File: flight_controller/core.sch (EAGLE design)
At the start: 119 parts, among them J1 M02, J10 M02, J11 M03, J12 M02, J13 M02, J14 M02, J15 M03, J16 M03, J17 M03, J18 M04, J19 M04, J2 M02, J20 M03, J21 M04, J3 M02, J4 M03, J5 M02, J6 M02, J7 M02, J8 M02, J9 M03, Q1 EM6K1, Q2 EM6K1, Q3 EM6K1, Q4 EM6K1, Q5 EM6K1, Q6 EM6K1, Q7 MOSFET-PCHANNEL-AON6407, U1 STM32F405, U2 MEAS-MS5611, U3 MPU-9250-QFN-24-NP, U4 MIC5219 3.3V, U5 USD-SOCKETNEW, Y1 16MHz

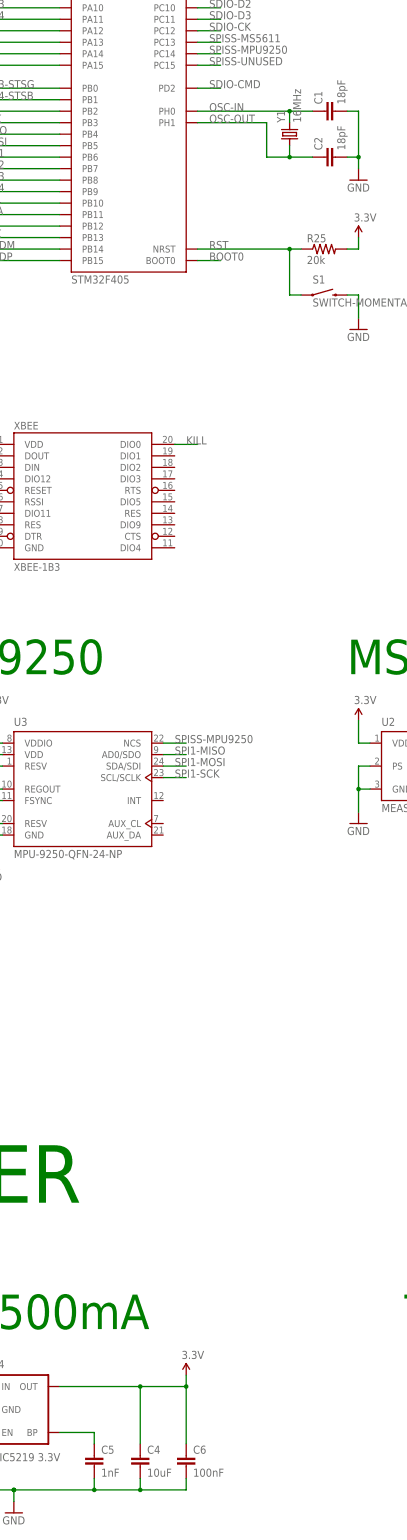
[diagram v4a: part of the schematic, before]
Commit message: Layout 70% done with new 8MHz crystal.
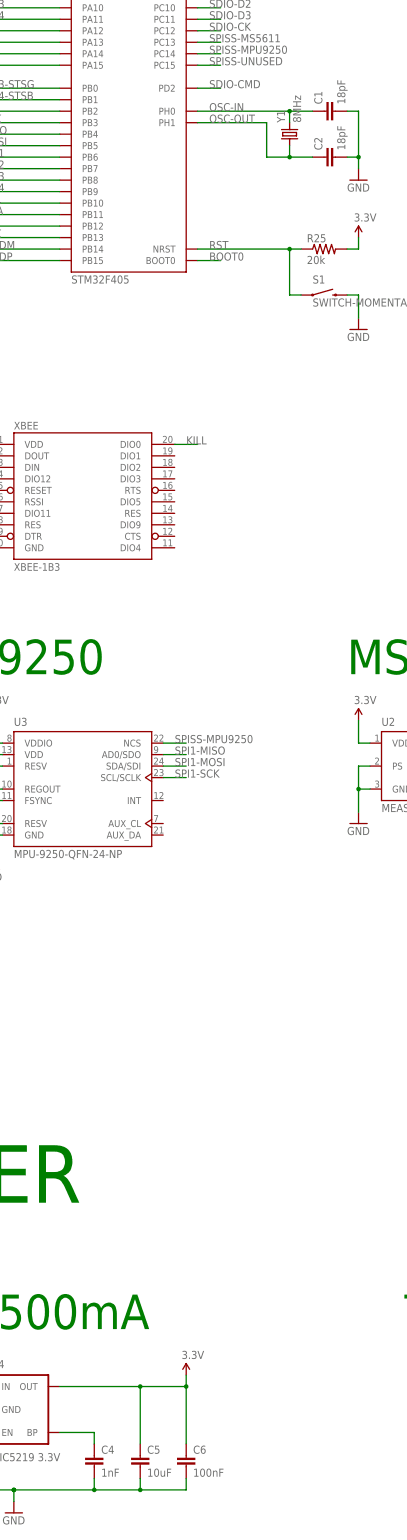
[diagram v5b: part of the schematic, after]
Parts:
- C4: value 10uF -> 1nF; device OSURC_Passives:CAP-10UF-10V-10%(0805) -> OSURC_Passives:CAP-1NF-50V-10%(0603)
- C5: value 1nF -> 10uF; device OSURC_Passives:CAP-1NF-50V-10%(0603) -> OSURC_Passives:CAP-10UF-10V-10%(0805)
- Y1: value 16MHz -> 8MHz; device SparkFun-FreqCtrl:CRYSTAL5X3 -> OSURC_FreqCtrl:CRYSTAL-8MHZ-CX532
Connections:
- net 3.3V: now also C5.2; no longer C4.2
- net MIC-BP: now also C4.2; no longer C5.2
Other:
- moved on the sheet: C4, C5
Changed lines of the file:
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@@
 <part name="C6" library="OSURC_Passives" deviceset="CAP" device="-100NF-16V-10%(0603)" value="100nF"/>
 <part name="U4" library="SparkFun-PowerIC" deviceset="V_REG_MIC5219" device="3.3V" value="MIC5219 3.3V"/>
-<part name="C5" library="OSURC_Passives" deviceset="CAP" device="-1NF-50V-10%(0603)" value="1nF"/>
+<part name="C4" library="OSURC_Passives" deviceset="CAP" device="-1NF-50V-10%(0603)" value="1nF"/>
 <part name="SUPPLY2" library="SparkFun-Aesthetics" deviceset="5V" device=""/>
 <part name="SUPPLY6" library="SparkFun-Aesthetics" deviceset="3.3V" device=""/>
@@
 <part name="R32" library="OSURC_Passives" deviceset="RES" device="-20KOHM-0.1W-1%(0603)" value="20k"/>
 <part name="GND25" library="SparkFun-Aesthetics" deviceset="GND" device=""/>
-<part name="Y1" library="SparkFun-FreqCtrl" deviceset="CRYSTAL" device="5X3" value="16MHz"/>
+<part name="Y1" library="OSURC_FreqCtrl" deviceset="CRYSTAL" device="-8MHZ-CX532" value="8MHz"/>
 <part name="C1" library="OSURC_Passives" deviceset="CAP" device="-18PF-50V-5%(0603)" value="18pF"/>
 <part name="C2" library="OSURC_Passives" deviceset="CAP" device="-18PF-50V-5%(0603)" value="18pF"/>
@@
 <part name="GND6" library="SparkFun-Aesthetics" deviceset="GND" device=""/>
 <part name="C3" library="OSURC_Passives" deviceset="CAP" device="-10UF-10V-10%(0805)" value="10uF"/>
-<part name="C4" library="OSURC_Passives" deviceset="CAP" device="-10UF-10V-10%(0805)" value="10uF"/>
+<part name="C5" library="OSURC_Passives" deviceset="CAP" device="-10UF-10V-10%(0805)" value="10uF"/>
 </parts>
 <sheets>
@@
 <instance part="C6" gate="G$1" x="81.28" y="-104.14"/>
 <instance part="U4" gate="G$1" x="45.72" y="-91.44"/>
-<instance part="C5" gate="G$1" x="60.96" y="-104.14"/>
+<instance part="C4" gate="G$1" x="60.96" y="-104.14"/>
 <instance part="SUPPLY2" gate="G$1" x="17.78" y="-83.82"/>
 <instance part="SUPPLY6" gate="G$1" x="81.28" y="-83.82"/>
@@
 <instance part="GND6" gate="1" x="363.22" y="-629.92"/>
 <instance part="C3" gate="G$1" x="17.78" y="-104.14"/>
-<instance part="C4" gate="G$1" x="71.12" y="-104.14"/>
+<instance part="C5" gate="G$1" x="71.12" y="-104.14"/>
 </instances>
 <busses>
@@
 <wire x1="17.78" y1="-109.22" x2="30.48" y2="-109.22" width="0.1524" layer="91"/>
 <junction x="30.48" y="-109.22"/>
-<pinref part="C5" gate="G$1" pin="1"/>
+<pinref part="C4" gate="G$1" pin="1"/>
 <wire x1="60.96" y1="-106.68" x2="60.96" y2="-109.22" width="0.1524" layer="91"/>
 <junction x="60.96" y="-109.22"/>
 <pinref part="GND8" gate="1" pin="GND"/>
 <pinref part="C3" gate="G$1" pin="1"/>
-<pinref part="C4" gate="G$1" pin="1"/>
+<pinref part="C5" gate="G$1" pin="1"/>
 </segment>
 <segment>
@@
 <pinref part="SUPPLY6" gate="G$1" pin="3.3V"/>
 <junction x="81.28" y="-86.36"/>
-<pinref part="C4" gate="G$1" pin="2"/>
+<pinref part="C5" gate="G$1" pin="2"/>
 </segment>
 <segment>
@@
 <segment>
 <pinref part="U4" gate="G$1" pin="BP"/>
-<pinref part="C5" gate="G$1" pin="2"/>
+<pinref part="C4" gate="G$1" pin="2"/>
 <wire x1="53.34" y1="-96.52" x2="60.96" y2="-96.52" width="0.1524" layer="91"/>
 <wire x1="60.96" y1="-96.52" x2="60.96" y2="-99.06" width="0.1524" layer="91"/>

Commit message: FC layout 90% done.
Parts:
- removed TP15: TEST-POINT-KEYSTONE-5019, OSURC_Passives:TEST-POINT-KEYSTONE-5019
- TP1, TP7, TP8: value TEST-POINT-KEYSTONE-5019 -> TEST-POINT-PAD.03C; device OSURC_Passives:TEST-POINT-KEYSTONE-5019 -> OSURC_Passives:TEST-POINT-PAD.03C
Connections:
- net OSC-IN: no longer TP15.1
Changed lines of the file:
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@@
 <part name="SUPPLY9" library="SparkFun-Aesthetics" deviceset="3.3V" device=""/>
 <part name="SUPPLY23" library="SparkFun-Aesthetics" deviceset="3.3V" device=""/>
-<part name="TP1" library="OSURC_Passives" deviceset="TEST-POINT" device="-KEYSTONE-5019"/>
+<part name="TP1" library="OSURC_Passives" deviceset="TEST-POINT" device="-PAD.03C" value="TEST-POINT-PAD.03C"/>
 <part name="TP2" library="OSURC_Passives" deviceset="TEST-POINT" device="-KEYSTONE-5019"/>
 <part name="TP3" library="OSURC_Passives" deviceset="TEST-POINT" device="-KEYSTONE-5019"/>
-<part name="TP7" library="OSURC_Passives" deviceset="TEST-POINT" device="-KEYSTONE-5019"/>
-<part name="TP8" library="OSURC_Passives" deviceset="TEST-POINT" device="-KEYSTONE-5019"/>
+<part name="TP7" library="OSURC_Passives" deviceset="TEST-POINT" device="-PAD.03C" value="TEST-POINT-PAD.03C"/>
+<part name="TP8" library="OSURC_Passives" deviceset="TEST-POINT" device="-PAD.03C" value="TEST-POINT-PAD.03C"/>
 <part name="TP9" library="OSURC_Passives" deviceset="TEST-POINT" device="-KEYSTONE-5019"/>
 <part name="TP10" library="OSURC_Passives" deviceset="TEST-POINT" device="-KEYSTONE-5019"/>
@@
 <part name="TP5" library="OSURC_Passives" deviceset="TEST-POINT" device="-PAD.03C"/>
 <part name="TP6" library="OSURC_Passives" deviceset="TEST-POINT" device="-PAD.03C"/>
-<part name="TP15" library="OSURC_Passives" deviceset="TEST-POINT" device="-KEYSTONE-5019"/>
 <part name="J6" library="OSURC_Connectors" deviceset="M02" device=""/>
 <part name="J10" library="OSURC_Connectors" deviceset="M02" device=""/>
@@
 <instance part="TP5" gate="G$1" x="246.38" y="-441.96"/>
 <instance part="TP6" gate="G$1" x="246.38" y="-449.58"/>
-<instance part="TP15" gate="G$1" x="246.38" y="-518.16"/>
 <instance part="J6" gate="G$1" x="40.64" y="-429.26"/>
 <instance part="J10" gate="G$1" x="40.64" y="-441.96"/>
@@
 <junction x="104.14" y="195.58"/>
 </segment>
-<segment>
-<wire x1="223.52" y1="-518.16" x2="246.38" y2="-518.16" width="0.1524" layer="91"/>
-<label x="223.52" y="-518.16" size="1.778" layer="95"/>
-<pinref part="TP15" gate="G$1" pin="1"/>
-</segment>
-</net>
+</net>

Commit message: Resolve all errors and finish routing.
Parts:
- C13: value 100nF -> 10uF; device OSURC_Passives:CAP-100NF-16V-10%(0603) -> OSURC_Passives:CAP-10UF-10V-10%(0805)
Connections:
- net 3.3V: now also C7.2; no longer C7.1
- net GND: now also C7.1; no longer C7.2
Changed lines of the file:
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@@
 <part name="SUPPLY7" library="SparkFun-Aesthetics" deviceset="3.3V" device=""/>
 <part name="GND20" library="SparkFun-Aesthetics" deviceset="GND" device=""/>
-<part name="C13" library="OSURC_Passives" deviceset="CAP" device="-100NF-16V-10%(0603)" value="100nF"/>
+<part name="C13" library="OSURC_Passives" deviceset="CAP" device="-10UF-10V-10%(0805)" value="10uF"/>
 <part name="SUPPLY8" library="SparkFun-Aesthetics" deviceset="3.3V" device=""/>
 <part name="GND21" library="SparkFun-Aesthetics" deviceset="GND" device=""/>
@@
 <wire x1="33.02" y1="-177.8" x2="25.4" y2="-177.8" width="0.1524" layer="91"/>
 <wire x1="25.4" y1="-177.8" x2="17.78" y2="-177.8" width="0.1524" layer="91"/>
-<wire x1="17.78" y1="-177.8" x2="17.78" y2="-167.64" width="0.1524" layer="91"/>
 <wire x1="88.9" y1="-175.26" x2="88.9" y2="-177.8" width="0.1524" layer="91"/>
 <wire x1="81.28" y1="-175.26" x2="81.28" y2="-177.8" width="0.1524" layer="91"/>
@@
 <wire x1="60.96" y1="-180.34" x2="60.96" y2="-177.8" width="0.1524" layer="91"/>
 <junction x="60.96" y="-177.8"/>
-<pinref part="C7" gate="G$1" pin="2"/>
 <pinref part="C11" gate="G$1" pin="1"/>
 <pinref part="C12" gate="G$1" pin="1"/>
@@
 <junction x="33.02" y="-177.8"/>
 <junction x="25.4" y="-177.8"/>
+<pinref part="C7" gate="G$1" pin="1"/>
+<wire x1="17.78" y1="-177.8" x2="17.78" y2="-175.26" width="0.1524" layer="91"/>
 </segment>
 <segment>
@@
 <wire x1="33.02" y1="-162.56" x2="25.4" y2="-162.56" width="0.1524" layer="91"/>
 <wire x1="25.4" y1="-162.56" x2="17.78" y2="-162.56" width="0.1524" layer="91"/>
-<pinref part="C7" gate="G$1" pin="1"/>
-<wire x1="17.78" y1="-175.26" x2="17.78" y2="-162.56" width="0.1524" layer="91"/>
 <junction x="43.18" y="-162.56"/>
 <pinref part="C10" gate="G$1" pin="2"/>
@@
 <junction x="33.02" y="-162.56"/>
 <junction x="40.64" y="-162.56"/>
+<pinref part="C7" gate="G$1" pin="2"/>
+<wire x1="17.78" y1="-167.64" x2="17.78" y2="-162.56" width="0.1524" layer="91"/>
 </segment>
 <segment>
@@
 <segment>
 <pinref part="Q4" gate="A" pin="G"/>
-<pinref part="Q4" gate="B" pin="G"/>
-<wire x1="345.44" y1="180.34" x2="345.44" y2="167.64" width="0.1524" layer="91"/>
 <wire x1="345.44" y1="167.64" x2="322.58" y2="167.64" width="0.1524" layer="91"/>
 <wire x1="322.58" y1="167.64" x2="322.58" y2="180.34" width="0.1524" layer="91"/>
@@
 <wire x1="322.58" y1="167.64" x2="312.42" y2="167.64" width="0.1524" layer="91"/>
 <junction x="322.58" y="167.64"/>
+<junction x="368.3" y="167.64"/>
+<pinref part="Q4" gate="B" pin="G"/>
+<wire x1="345.44" y1="167.64" x2="345.44" y2="180.34" width="0.1524" layer="91"/>
 <junction x="345.44" y="167.64"/>
-<junction x="368.3" y="167.64"/>
 </segment>
 </net>

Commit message: Add USB diffpair net class and USB termination resistors.
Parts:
- added R37: 1.5k, OSURC_Passives:RES-1.5KOHM-0.1W-5%(0603)
- added R38, R39: 22, OSURC_Passives:RES-22OHM-0.1W-5%(0603)
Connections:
- removed net OTG-HS-DM: JP1.D-, TP7.1, U1.GPIO.PB14
- removed net OTG-HS-DP: JP1.D+, TP8.1, U1.GPIO.PB15
- new net OTG-HS-D'_N: R39.1, U1.GPIO.PB14
- new net OTG-HS-D'_P: R37.1, R38.1, U1.GPIO.PB15
- new net OTG-HS-D_N: JP1.D-, R39.2, TP7.1
- new net OTG-HS-D_P: JP1.D+, R38.2, TP8.1
- net 3.3V: now also R37.2
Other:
- moved on the sheet: J21, JP1
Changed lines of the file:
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@@
 <?xml version="1.0" encoding="utf-8"?>
 <!DOCTYPE eagle SYSTEM "eagle.dtd">
-<eagle version="7.1.0">
+<eagle version="7.2.0">
 <drawing>
 <settings>
@@
 <classes>
 <class number="0" name="default" width="0" drill="0">
+</class>
+<class number="1" name="USB" width="0.6096" drill="0">
 </class>
 </classes>
@@
 <part name="C3" library="OSURC_Passives" deviceset="CAP" device="-10UF-10V-10%(0805)" value="10uF"/>
 <part name="C5" library="OSURC_Passives" deviceset="CAP" device="-10UF-10V-10%(0805)" value="10uF"/>
+<part name="R37" library="OSURC_Passives" deviceset="RES" device="-1.5KOHM-0.1W-5%(0603)" value="1.5k"/>
+<part name="SUPPLY24" library="SparkFun-Aesthetics" deviceset="3.3V" device=""/>
+<part name="R38" library="OSURC_Passives" deviceset="RES" device="-22OHM-0.1W-5%(0603)" value="22"/>
+<part name="R39" library="OSURC_Passives" deviceset="RES" device="-22OHM-0.1W-5%(0603)" value="22"/>
 </parts>
 <sheets>
@@
 <text x="106.68" y="-487.68" size="7.62" layer="91">UART</text>
 <text x="15.24" y="-403.86" size="7.62" layer="91">PWM</text>
-<text x="132.08" y="-563.88" size="7.62" layer="91">SWD</text>
+<text x="83.82" y="-563.88" size="7.62" layer="91">SWD</text>
 <text x="312.42" y="256.54" size="7.62" layer="91">KILL</text>
 <text x="15.24" y="256.54" size="7.62" layer="91">STM32F4</text>
@@
 <frame x1="0" y1="-330.2" x2="431.8" y2="-50.8" columns="8" rows="5" layer="91"/>
 <text x="15.24" y="-190.5" size="1.778" layer="98">Place caps near VDD and VCAP pads</text>
-<text x="81.28" y="-563.88" size="7.62" layer="91">USB</text>
+<text x="124.46" y="-563.88" size="7.62" layer="91">USB</text>
 <text x="15.24" y="243.84" size="1.778" layer="98">AF TIM2</text>
 <text x="15.24" y="185.42" size="1.778" layer="98">AF UART1</text>
@@
 <instance part="R9" gate="G$1" x="144.78" y="228.6"/>
 <instance part="LED3" gate="G$1" x="154.94" y="228.6" rot="R90"/>
-<instance part="JP1" gate="G$1" x="106.68" y="-586.74"/>
-<instance part="GND10" gate="1" x="99.06" y="-594.36"/>
+<instance part="JP1" gate="G$1" x="182.88" y="-596.9"/>
+<instance part="GND10" gate="1" x="175.26" y="-604.52"/>
 <instance part="SUPPLY15" gate="G$1" x="40.64" y="-574.04"/>
 <instance part="GND11" gate="1" x="40.64" y="-622.3"/>
@@
 <instance part="J18" gate="G$1" x="35.56" y="-502.92"/>
 <instance part="J19" gate="G$1" x="175.26" y="-508"/>
-<instance part="J21" gate="G$1" x="149.86" y="-579.12"/>
+<instance part="J21" gate="G$1" x="101.6" y="-579.12"/>
 <instance part="J2" gate="G$1" x="81.28" y="-416.56"/>
-<instance part="SUPPLY1" gate="G$1" x="99.06" y="-574.04"/>
+<instance part="SUPPLY1" gate="G$1" x="175.26" y="-584.2"/>
 <instance part="J11" gate="G$1" x="81.28" y="-441.96"/>
 <instance part="J15" gate="G$1" x="81.28" y="-457.2"/>
@@
 <instance part="C3" gate="G$1" x="17.78" y="-104.14"/>
 <instance part="C5" gate="G$1" x="71.12" y="-104.14"/>
+<instance part="R37" gate="G$1" x="142.24" y="-579.12" rot="R90"/>
+<instance part="SUPPLY24" gate="G$1" x="142.24" y="-574.04"/>
+<instance part="R38" gate="G$1" x="149.86" y="-589.28"/>
+<instance part="R39" gate="G$1" x="149.86" y="-596.9"/>
 </instances>
 <busses>
@@
 <net name="GND" class="0">
 <segment>
-<wire x1="144.78" y1="-581.66" x2="132.08" y2="-581.66" width="0.1524" layer="91"/>
-<label x="132.08" y="-581.66" size="1.778" layer="95"/>
+<wire x1="96.52" y1="-581.66" x2="83.82" y2="-581.66" width="0.1524" layer="91"/>
+<label x="83.82" y="-581.66" size="1.778" layer="95"/>
 <pinref part="J21" gate="G$1" pin="4"/>
 </segment>
@@
 <segment>
 <pinref part="JP1" gate="G$1" pin="GND"/>
-<wire x1="104.14" y1="-586.74" x2="99.06" y2="-586.74" width="0.1524" layer="91"/>
-<wire x1="99.06" y1="-586.74" x2="99.06" y2="-591.82" width="0.1524" layer="91"/>
+<wire x1="180.34" y1="-596.9" x2="175.26" y2="-596.9" width="0.1524" layer="91"/>
+<wire x1="175.26" y1="-596.9" x2="175.26" y2="-601.98" width="0.1524" layer="91"/>
 <pinref part="GND10" gate="1" pin="GND"/>
 </segment>
@@
 <net name="RST" class="0">
 <segment>
-<wire x1="144.78" y1="-574.04" x2="132.08" y2="-574.04" width="0.1524" layer="91"/>
-<label x="132.08" y="-574.04" size="1.778" layer="95"/>
+<wire x1="96.52" y1="-574.04" x2="83.82" y2="-574.04" width="0.1524" layer="91"/>
+<label x="83.82" y="-574.04" size="1.778" layer="95"/>
 <pinref part="J21" gate="G$1" pin="1"/>
 </segment>
@@
 <pinref part="SUPPLY9" gate="G$1" pin="3.3V"/>
 </segment>
+<segment>
+<pinref part="R37" gate="G$1" pin="2"/>
+<pinref part="SUPPLY24" gate="G$1" pin="3.3V"/>
+</segment>
 </net>
 <net name="KILL" class="0">
@@
 </segment>
 </net>
-<net name="OTG-HS-DP" class="0">
-<segment>
-<wire x1="53.34" y1="162.56" x2="30.48" y2="162.56" width="0.1524" layer="91"/>
-<label x="30.48" y="162.56" size="1.778" layer="95"/>
-<pinref part="U1" gate=".GPIO" pin="PB15"/>
-</segment>
-<segment>
-<wire x1="104.14" y1="-579.12" x2="81.28" y2="-579.12" width="0.1524" layer="91"/>
-<label x="81.28" y="-579.12" size="1.778" layer="95"/>
-<pinref part="JP1" gate="G$1" pin="D+"/>
-</segment>
-<segment>
-<wire x1="246.38" y1="-464.82" x2="223.52" y2="-464.82" width="0.1524" layer="91"/>
-<label x="223.52" y="-464.82" size="1.778" layer="95"/>
-<pinref part="TP8" gate="G$1" pin="1"/>
-</segment>
-</net>
 <net name="TIM3-CH3-STSG" class="0">
 <segment>
@@
 <label x="381" y="203.2" size="1.778" layer="95"/>
 <wire x1="375.92" y1="203.2" x2="383.54" y2="203.2" width="0.1524" layer="91"/>
-</segment>
-</net>
-<net name="OTG-HS-DM" class="0">
-<segment>
-<wire x1="53.34" y1="165.1" x2="30.48" y2="165.1" width="0.1524" layer="91"/>
-<label x="30.48" y="165.1" size="1.778" layer="95"/>
-<pinref part="U1" gate=".GPIO" pin="PB14"/>
-</segment>
-<segment>
-<wire x1="104.14" y1="-581.66" x2="81.28" y2="-581.66" width="0.1524" layer="91"/>
-<label x="81.28" y="-581.66" size="1.778" layer="95"/>
-<pinref part="JP1" gate="G$1" pin="D-"/>
-</segment>
-<segment>
-<wire x1="246.38" y1="-457.2" x2="223.52" y2="-457.2" width="0.1524" layer="91"/>
-<label x="223.52" y="-457.2" size="1.778" layer="95"/>
-<pinref part="TP7" gate="G$1" pin="1"/>
 </segment>
 </net>
@@
 </segment>
 <segment>
-<wire x1="144.78" y1="-576.58" x2="132.08" y2="-576.58" width="0.1524" layer="91"/>
-<label x="132.08" y="-576.58" size="1.778" layer="95"/>
+<wire x1="96.52" y1="-576.58" x2="83.82" y2="-576.58" width="0.1524" layer="91"/>
+<label x="83.82" y="-576.58" size="1.778" layer="95"/>
 <pinref part="J21" gate="G$1" pin="2"/>
 </segment>
@@
 </segment>
 <segment>
-<wire x1="144.78" y1="-579.12" x2="132.08" y2="-579.12" width="0.1524" layer="91"/>
-<label x="132.08" y="-579.12" size="1.778" layer="95"/>
+<wire x1="96.52" y1="-579.12" x2="83.82" y2="-579.12" width="0.1524" layer="91"/>
+<label x="83.82" y="-579.12" size="1.778" layer="95"/>
 <pinref part="J21" gate="G$1" pin="3"/>
 </segment>
@@
 <segment>
 <pinref part="JP1" gate="G$1" pin="VBUS"/>
-<wire x1="104.14" y1="-584.2" x2="99.06" y2="-584.2" width="0.1524" layer="91"/>
-<wire x1="99.06" y1="-584.2" x2="99.06" y2="-574.04" width="0.1524" layer="91"/>
+<wire x1="180.34" y1="-594.36" x2="175.26" y2="-594.36" width="0.1524" layer="91"/>
+<wire x1="175.26" y1="-594.36" x2="175.26" y2="-584.2" width="0.1524" layer="91"/>
 <pinref part="SUPPLY1" gate="G$1" pin="VIN"/>
 </segment>
@@
 </segment>
 </net>
+<net name="OTG-HS-D_N" class="1">
+<segment>
+<wire x1="180.34" y1="-591.82" x2="157.48" y2="-591.82" width="0.1524" layer="91"/>
+<wire x1="157.48" y1="-591.82" x2="157.48" y2="-596.9" width="0.1524" layer="91"/>
+<wire x1="157.48" y1="-596.9" x2="154.94" y2="-596.9" width="0.1524" layer="91"/>
+<label x="157.48" y="-591.82" size="1.778" layer="95"/>
+<pinref part="JP1" gate="G$1" pin="D-"/>
+<pinref part="R39" gate="G$1" pin="2"/>
+</segment>
+<segment>
+<wire x1="246.38" y1="-457.2" x2="223.52" y2="-457.2" width="0.1524" layer="91"/>
+<label x="223.52" y="-457.2" size="1.778" layer="95"/>
+<pinref part="TP7" gate="G$1" pin="1"/>
+</segment>
+</net>
+<net name="OTG-HS-D_P" class="1">
+<segment>
+<wire x1="180.34" y1="-589.28" x2="154.94" y2="-589.28" width="0.1524" layer="91"/>
+<label x="157.48" y="-589.28" size="1.778" layer="95"/>
+<pinref part="JP1" gate="G$1" pin="D+"/>
+<pinref part="R38" gate="G$1" pin="2"/>
+</segment>
+<segment>
+<wire x1="246.38" y1="-464.82" x2="223.52" y2="-464.82" width="0.1524" layer="91"/>
+<label x="223.52" y="-464.82" size="1.778" layer="95"/>
+<pinref part="TP8" gate="G$1" pin="1"/>
+</segment>
+</net>
+<net name="OTG-HS-D'_N" class="1">
+<segment>
+<wire x1="53.34" y1="165.1" x2="30.48" y2="165.1" width="0.1524" layer="91"/>
+<label x="30.48" y="165.1" size="1.778" layer="95"/>
+<pinref part="U1" gate=".GPIO" pin="PB14"/>
+</segment>
+<segment>
+<wire x1="124.46" y1="-596.9" x2="144.78" y2="-596.9" width="0.1524" layer="91"/>
+<label x="124.46" y="-596.9" size="1.778" layer="95"/>
+<pinref part="R39" gate="G$1" pin="1"/>
+</segment>
+</net>
+<net name="OTG-HS-D'_P" class="1">
+<segment>
+<wire x1="53.34" y1="162.56" x2="30.48" y2="162.56" width="0.1524" layer="91"/>
+<label x="30.48" y="162.56" size="1.778" layer="95"/>
+<pinref part="U1" gate=".GPIO" pin="PB15"/>
+</segment>
+<segment>
+<wire x1="124.46" y1="-589.28" x2="142.24" y2="-589.28" width="0.1524" layer="91"/>
+<label x="124.46" y="-589.28" size="1.778" layer="95"/>
+<wire x1="142.24" y1="-589.28" x2="144.78" y2="-589.28" width="0.1524" layer="91"/>
+<wire x1="142.24" y1="-589.28" x2="142.24" y2="-584.2" width="0.1524" layer="91"/>
+<junction x="142.24" y="-589.28"/>
+<pinref part="R37" gate="G$1" pin="1"/>
+<pinref part="R38" gate="G$1" pin="1"/>
+</segment>
+</net>
